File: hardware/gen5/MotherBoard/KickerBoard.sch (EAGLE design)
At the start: 151 parts

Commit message: Mainboard placement concept completed. Still need to add motor board power connectors
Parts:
- removed JP1, JP2, JP3, JP4: (no value), SparkFun-Connectors:M04SMD_RA_FEMALE
- removed U$10, U$11, U$8, U$9: 2X5HEAD, Teensy356:2X5HEAD
- added J1, J2, J3, J4: (no value), SparkFun-Connectors:M05X2SHD
- added J5, J6, J7, J8: (no value), SparkFun-Connectors:M04PTH
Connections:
- net 5V: now also J5.1, J6.1, J7.1, J8.1; no longer JP1.4, JP2.4, JP3.4, JP4.4
- net BREN0: now also J1.6; no longer U$10.8
- net BREN1: now also J3.6; no longer U$9.8
- net BREN2: now also J4.6; no longer U$8.8
- net BREN3: now also J2.6; no longer U$11.8
- net DIR0: now also J1.8; no longer U$10.7
- net DIR1: now also J3.4; no longer U$9.9
- net DIR2: now also J4.4; no longer U$8.9
- net DIR3: now also J2.8; no longer U$11.7
- net ENABLE0: now also J1.4; no longer U$10.9
- net ENABLE1: now also J3.8; no longer U$9.7
- net ENABLE2: now also J4.8; no longer U$8.7
- net ENABLE3: now also J2.4; no longer U$11.9
- net FAULT0: now also J1.2; no longer U$10.10
- net FAULT1: now also J3.10; no longer U$9.6
- net FAULT2: now also J4.10; no longer U$8.6
- net FAULT3: now also J2.2; no longer U$11.10
- net GND: now also J1.9, J2.9, J3.1, J4.1, J5.3, J6.3, J7.3, J8.3; no longer JP1.2, JP2.2, JP3.2, JP4.2, U$10.5, U$11.5, U$8.1, U$9.1
- net HALLOUT0: now also J1.1; no longer U$10.1
- net HALLOUT1: now also J3.9; no longer U$9.5
- net HALLOUT2: now also J4.9; no longer U$8.5
- net HALLOUT3: now also J2.1; no longer U$11.1
- net LOCKN0: now also J1.10; no longer U$10.6
- net LOCKN1: now also J3.2; no longer U$9.10
- net LOCKN2: now also J4.2; no longer U$8.10
- net LOCKN3: now also J2.10; no longer U$11.6
- net M1QA-1: now also J5.2; no longer JP4.3, U$14.27
- net M1QA-1OUT: now also U$14.27
- net M1QA-2: now also J6.2; no longer JP1.3, U$14.17/A3
- net M1QA-2OUT: now also U$14.17/A3
- net M1QA-3: now also J7.2; no longer JP2.3, U$14.15/A1
- net M1QA-3OUT: now also U$14.15/A1
- net M1QA-4: now also J8.2; no longer JP3.3, U$14.25
- net M1QA-4OUT: now also U$14.25
- net M1QB-1: now also J5.4; no longer JP4.1, U$14.28
- net M1QB-1OUT: now also U$14.28
- net M1QB-2: now also J6.4; no longer JP1.1, U$14.16/A2
- net M1QB-2OUT: now also U$14.16/A2
- net M1QB-3: now also J7.4; no longer JP2.1, U$14.14/A0
- net M1QB-3OUT: now also U$14.14/A0
- net M1QB-4: now also J8.4; no longer JP3.1, U$14.26
- net M1QB-4OUT: now also U$14.26
- net PWM0: now also J1.3; no longer U$10.2
- net PWM1: now also J3.7; no longer U$9.4
- net PWM2: now also J4.7; no longer U$8.4
- net PWM3: now also J2.3; no longer U$11.2

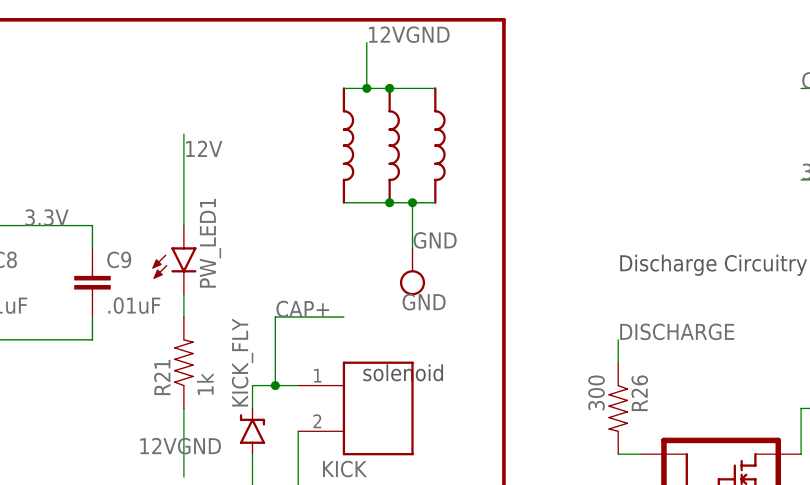
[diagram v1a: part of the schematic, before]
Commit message: re-routed 3.3V bus
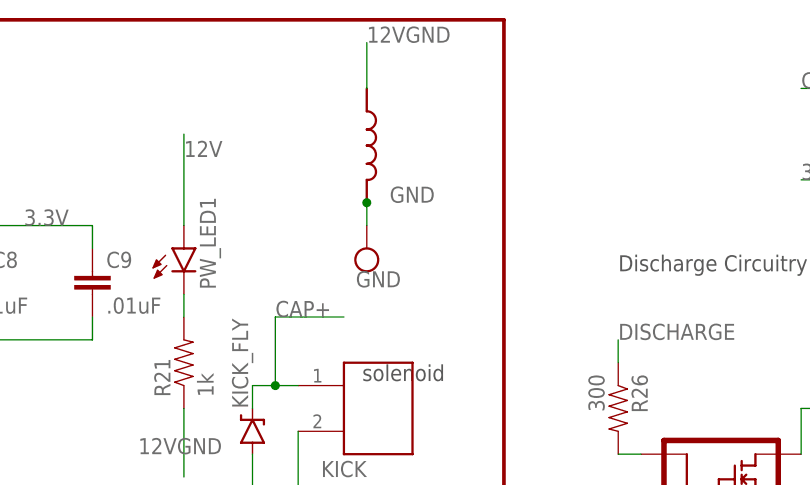
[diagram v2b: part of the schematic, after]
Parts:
- removed U$13, U$20: INDUCTOR, gen3:INDUCTOR
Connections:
- net 12VGND: no longer U$13.P$1, U$20.P$1
- net GND: no longer U$13.P$2, U$20.P$2
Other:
- moved on the sheet: GND
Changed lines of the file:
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@@
 <part name="R22" library="SparkFun-Passives" deviceset="RESISTOR" device="0805-RES" value="100k"/>
 <part name="U$12" library="rfc" deviceset="13VZENER" device=""/>
-<part name="U$13" library="gen3" deviceset="INDUCTOR" device=""/>
 <part name="R37" library="SparkFun-Passives" deviceset="RESISTOR" device="0805-RES" value="100k"/>
 <part name="U$18" library="foe-scale" deviceset="LM311" device=""/>
 <part name="C33" library="SparkFun-Capacitors" deviceset="CAP" device="1206" value="1uF"/>
 <part name="U$19" library="gen3" deviceset="INDUCTOR" device=""/>
-<part name="U$20" library="gen3" deviceset="INDUCTOR" device=""/>
 <part name="C34" library="SparkFun-Capacitors" deviceset="CAP" device="1206" value="47uF"/>
 <part name="R43" library="SparkFun-Passives" deviceset="RESISTOR" device="0805-RES" value="100"/>
@@
 <instance part="DONE" gate="G$1" x="617.22" y="320.04"/>
 <instance part="GATE" gate="G$1" x="688.34" y="317.5"/>
-<instance part="GND" gate="G$1" x="497.84" y="350.52" rot="R180"/>
+<instance part="GND" gate="G$1" x="492.76" y="353.06" rot="R180"/>
 <instance part="12VGND" gate="G$1" x="754.38" y="248.92" rot="R270"/>
 <instance part="C6" gate="G$1" x="665.48" y="358.14"/>
@@
 <instance part="R22" gate="G$1" x="612.14" y="312.42"/>
 <instance part="U$12" gate="G$1" x="396.24" y="353.06" rot="R180"/>
-<instance part="U$13" gate="G$1" x="500.38" y="370.84" rot="R270"/>
 <instance part="R37" gate="G$1" x="284.48" y="304.8"/>
 <instance part="U$18" gate="G$1" x="325.12" y="307.34"/>
 <instance part="C33" gate="G$1" x="332.74" y="332.74"/>
-<instance part="U$19" gate="G$1" x="490.22" y="370.84" rot="R270"/>
-<instance part="U$20" gate="G$1" x="495.3" y="370.84" rot="R270"/>
+<instance part="U$19" gate="G$1" x="492.76" y="370.84" rot="R270"/>
 <instance part="C34" gate="G$1" x="744.22" y="259.08"/>
 <instance part="R43" gate="G$1" x="678.18" y="294.64"/>
@@
 <segment>
 <pinref part="U$19" gate="G$1" pin="P$2"/>
-<pinref part="U$20" gate="G$1" pin="P$2"/>
-<wire x1="495.3" y1="358.14" x2="490.22" y2="358.14" width="0.1524" layer="91"/>
-<pinref part="U$13" gate="G$1" pin="P$2"/>
-<wire x1="495.3" y1="358.14" x2="497.84" y2="358.14" width="0.1524" layer="91"/>
-<junction x="495.3" y="358.14"/>
-<wire x1="497.84" y1="358.14" x2="500.38" y2="358.14" width="0.1524" layer="91"/>
-<wire x1="497.84" y1="358.14" x2="497.84" y2="353.06" width="0.1524" layer="91"/>
-<junction x="497.84" y="358.14"/>
-<label x="497.84" y="353.06" size="1.778" layer="95"/>
+<wire x1="492.76" y1="358.14" x2="492.76" y2="355.6" width="0.1524" layer="91"/>
+<junction x="492.76" y="358.14"/>
+<label x="495.3" y="358.14" size="1.778" layer="95"/>
 <pinref part="GND" gate="G$1" pin="P$1"/>
 </segment>
@@
 </segment>
 <segment>
-<pinref part="U$13" gate="G$1" pin="P$1"/>
 <pinref part="U$19" gate="G$1" pin="P$1"/>
-<wire x1="495.3" y1="370.84" x2="500.38" y2="370.84" width="0.1524" layer="91"/>
-<junction x="495.3" y="370.84"/>
-<pinref part="U$20" gate="G$1" pin="P$1"/>
-<wire x1="495.3" y1="370.84" x2="492.76" y2="370.84" width="0.1524" layer="91"/>
-<wire x1="492.76" y1="370.84" x2="490.22" y2="370.84" width="0.1524" layer="91"/>
 <wire x1="492.76" y1="370.84" x2="492.76" y2="375.92" width="0.1524" layer="91"/>
-<junction x="492.76" y="370.84"/>
 <label x="492.76" y="375.92" size="1.778" layer="95"/>
 </segment>

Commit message: Completed Motherboard layout for current schematic. Need to add power connectors and drills for motorboard mounting
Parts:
- removed MOTOR1, MOTOR4: M20X2SHROUDED_SMT, SparkFun-Connectors:M20X2SHROUDED_SMT
- added C13: 100nF, SparkFun-Capacitors:CAP0805
- added R32: 200k, SparkFun-Resistors:RESISTOR0805-RES
- added R33, R34: 4.7k, SparkFun-Resistors:RESISTOR0805-RES
- added U$8: PCA9306, SparkFun-AnalogIC:PCA9306
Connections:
- new net N$38: C13.2, R32.1, U$8.EN, U$8.VREF2
- new net SCL-H: R33.1, U$17.SCK, U$21.SCK, U$8.SCL2
- new net SDA-H: R34.1, U$17.SDA, U$21.SDA, U$8.SDA2
- net 3.3V: now also U$8.VREF1; no longer C35.1, C36.1, C37.1, C38.1, U$17.RESET/, U$17.VDD, U$21.A2, U$21.RESET/, U$21.VDD
- net 5V: now also C35.1, C36.1, C37.1, C38.1, R32.2, R33.2, R34.2, U$17.RESET/, U$17.VDD, U$21.A2, U$21.RESET/, U$21.VDD
- net GND: now also C13.1, U$8.GND
- net SCL: now also U$8.SCL1; no longer U$17.SCK, U$21.SCK
- net SDA: now also U$8.SDA1; no longer U$17.SDA, U$21.SDA
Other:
- note removed: "There are 8 Quad Encoder Signals (MXQY) where X refers to the motor number (0-3) and Y referse to the signal (A or B)."
- moved on the sheet: 5REG, BAT, BATCLAMP2, BB_CON, C1, C10, C12, C35, C36, C37, C38, C39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

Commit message: Small motherboard changes
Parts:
- removed FRAME4: FRAME-LETTER, SparkFun-Aesthetics:FRAME-LETTER
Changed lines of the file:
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@@
 </classes>
 <parts>
-<part name="FRAME4" library="SparkFun-Aesthetics" deviceset="FRAME-LETTER" device=""/>
 <part name="R14" library="SparkFun-Resistors" deviceset="RESISTOR" device="0805-RES" value="1M"/>
 <part name="R15" library="SparkFun-Resistors" deviceset="RESISTOR" device="0805-RES" value="10K"/>
@@
 </plain>
 <instances>
-<instance part="FRAME4" gate="G$1" x="259.08" y="193.04"/>
-<instance part="FRAME4" gate="V" x="406.4" y="193.04"/>
 <instance part="R14" gate="G$1" x="779.78" y="353.06" rot="MR90"/>
 <instance part="R15" gate="G$1" x="779.78" y="330.2" rot="MR90"/>

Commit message: reformatted motherboard schematic into functional blocks
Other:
- note removed: "Differential Amplifier: Needed since the DAC on the MCU has a minimum output voltage of ~0.5V, but we want KICK_REF to range from approximately 0 to 2.5 V"
- note removed: "P8, P9, P10 are for Hall Sensors outputs... needed for proper operation of motor controller"
- moved on the sheet: 12V, 3.3REG1, 3.3V, 5REG, BAT, BATCLAMP2, BATT-1, BATT-2, C11, C39, C40, C41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

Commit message: minor mother board changes
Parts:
- added U$10, U$9: MOTOR, rfc:MOTOR
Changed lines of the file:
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@@
 <part name="R34" library="SparkFun-Resistors" deviceset="RESISTOR" device="0805-RES" value="4.7k"/>
 <part name="C13" library="SparkFun-Capacitors" deviceset="CAP" device="0805" value="100nF"/>
+<part name="U$9" library="rfc" deviceset="MOTOR" device=""/>
+<part name="U$10" library="rfc" deviceset="MOTOR" device=""/>
 </parts>
 <sheets>
@@
 <instance part="R34" gate="G$1" x="474.98" y="132.08" rot="R90"/>
 <instance part="C13" gate="G$1" x="449.58" y="134.62" rot="R90"/>
+<instance part="U$9" gate="G$1" x="218.44" y="279.4"/>
+<instance part="U$10" gate="G$1" x="218.44" y="243.84"/>
 </instances>
 <busses>

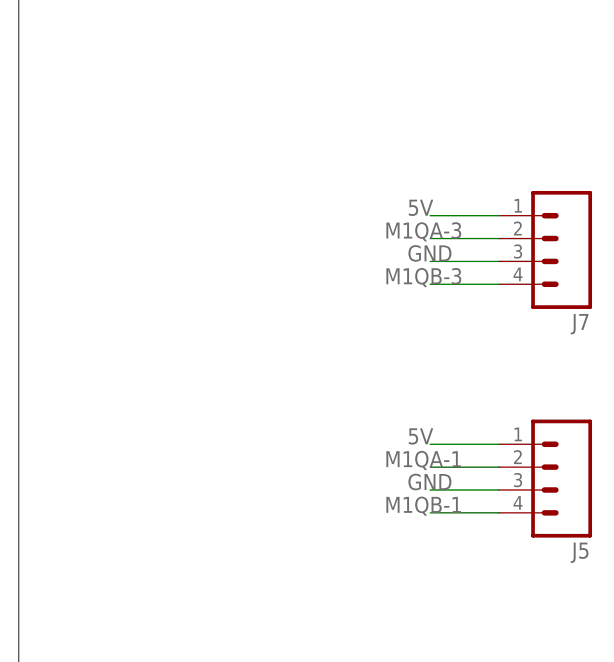
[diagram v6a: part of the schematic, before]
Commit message: Updated trace width on kicker path
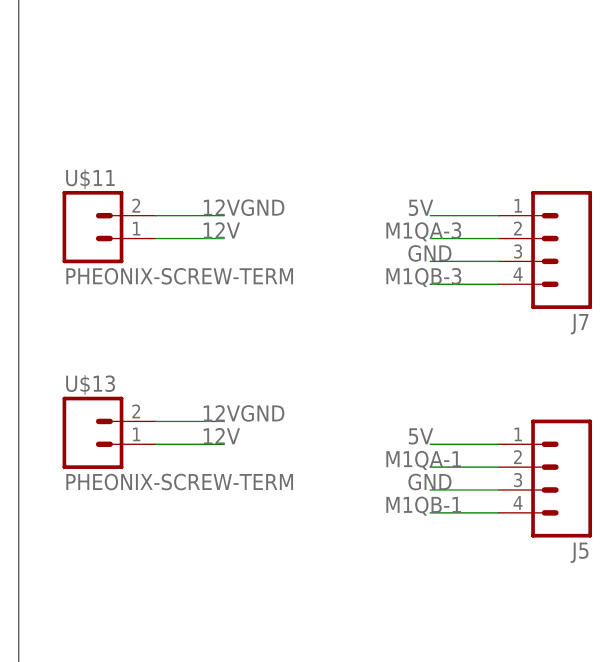
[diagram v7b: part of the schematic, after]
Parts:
- added U$11, U$13: PHEONIX-SCREW-TERM, SparkFun-Connectors:PHEONIX-SCREW-TERM
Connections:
- net 12V: now also U$11.1, U$13.1
- net 12VGND: now also U$11.2, U$13.2
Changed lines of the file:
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@@
 <part name="U$9" library="rfc" deviceset="MOTOR" device=""/>
 <part name="U$10" library="rfc" deviceset="MOTOR" device=""/>
+<part name="U$11" library="SparkFun-Connectors" deviceset="PHEONIX-SCREW-TERM" device=""/>
+<part name="U$13" library="SparkFun-Connectors" deviceset="PHEONIX-SCREW-TERM" device=""/>
 </parts>
 <sheets>
@@
 <instance part="U$9" gate="G$1" x="218.44" y="279.4"/>
 <instance part="U$10" gate="G$1" x="218.44" y="243.84"/>
+<instance part="U$11" gate="G$1" x="99.06" y="259.08"/>
+<instance part="U$13" gate="G$1" x="99.06" y="236.22"/>
 </instances>
 <busses>
@@
 <label x="820.42" y="350.52" size="1.778" layer="95" rot="MR0"/>
 </segment>
+<segment>
+<pinref part="U$13" gate="G$1" pin="2"/>
+<wire x1="106.68" y1="238.76" x2="114.3" y2="238.76" width="0.1524" layer="91"/>
+<label x="111.76" y="238.76" size="1.778" layer="95"/>
+</segment>
+<segment>
+<pinref part="U$11" gate="G$1" pin="2"/>
+<wire x1="106.68" y1="261.62" x2="114.3" y2="261.62" width="0.1524" layer="91"/>
+<label x="111.76" y="261.62" size="1.778" layer="95"/>
+</segment>
 </net>
 <net name="COMP_OUT" class="0">
@@
 <label x="487.68" y="459.74" size="1.778" layer="95"/>
 </segment>
-</net>
+<segment>
+<pinref part="U$13" gate="G$1" pin="1"/>
+<wire x1="106.68" y1="236.22" x2="114.3" y2="236.22" width="0.1524" layer="91"/>
+<label x="111.76" y="236.22" size="1.778" layer="95"/>
+</segment>
+<segment>
+<pinref part="U$11" gate="G$1" pin="1"/>
+<wire x1="106.68" y1="259.08" x2="114.3" y2="259.08" width="0.1524" layer="91"/>
+<label x="111.76" y="259.08" size="1.778" layer="95"/>
+</segment>
+</net>
